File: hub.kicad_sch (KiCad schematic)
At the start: 26 parts, among them J1 USB_C_Receptacle_USB2.0_16P, Q1 2N7002, Q2 2N7002, U1 ADuM4165, U2 USBLC6-2SC6, U3 TLV7042DDFR, Y1 24MHz

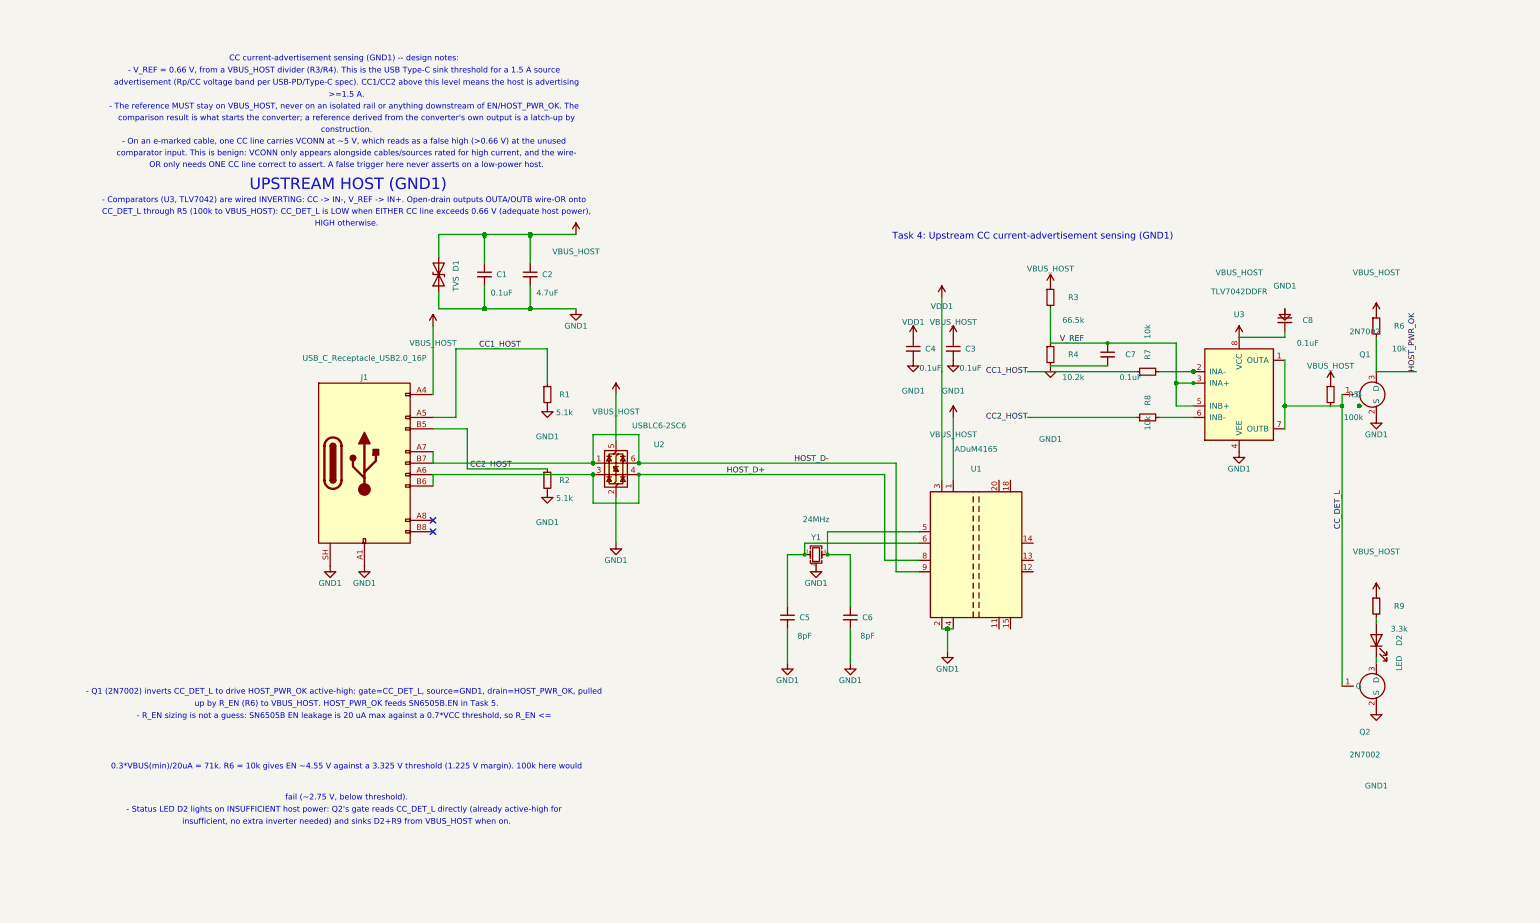
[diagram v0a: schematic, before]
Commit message: feat(revb/sch): SN6505B isolated DC-DC gated by host CC sense
Task 5 of the revb-hub-schematic plan — the isolated power chain and
first GND2-domain circuitry (push-pull converter, rectifier, buck-boost).

- U5 (SN6505BDBV) push-pull driver: VCC/GND on GND1 via C10 (0.1uF bypass)
  + C11 (4.7uF mandatory VCC bulk); EN <- HOST_PWR_OK (the change from both
  predecessor boards, which tied EN to VBUS permanently).
- T1 (750313638) transformer bridges GND1 (primary) to GND2 (secondary,
  CT2 -> GND2). C12 centre-tap bulk trimmed to 0.1uF (see budget below).
- D3/D4 (SS34, Device:D_Schottky) full-wave centre-tap rectifier into
  DCDC_RAW, side by side per the brief.
- U6 (TPS630701RNMR, fixed 5.0V buck-boost) — new custom symbol +
  placeholder footprint in isolator-lib, pin table per the decision
  record's Sec 2.4: FB tied to VOUT via R_FB0=0R (fixed-part requirement,
  not optional); PS/SYNC via R_PSS=100k to ISO_5V_PRE with a DNP 0R pad
  wired to the PS/SYNC node (not to ISO_5V_PRE — rev 2's wording would
  have shorted the rail to GND2 if that pad were ever fitted); EN tied to
  DCDC_RAW, not ISO_5V_PRE; VSEL tied to GND2; PG pulled up 100k; FB2 left
  open. Support caps (C_IN/C_IN-HF/C_OUT/C_OUT-HF/C_VAUX) and inductor L1
  per the decision record's table. R13/R2 (523k/100k) DNP footprints laid
  out for the adjustable-part fallback, tied to the FB node.
- Output net is ISO_5V_PRE (per the decision record's naming, not the
  brief's DCDC_5V — ISO_5V is reserved for the Task 6 TPS2121 output).

Capacitance budget: C1+C2+C3 (4.9uF, Task 3) + C10+C11+C12 (0.1+4.7+0.1)
= 9.8uF on VBUS_HOST, under the 10uF ceiling — C12 was the lever, reduced
from 4.7uF to 0.1uF as the brief anticipated.

Verification: kicad-cli netlist parse gate green after every batch; ERC
79 violations (18 errors), all baseline-consistent (PWR_FLAG-pending on
every new power net plus the pre-existing ones, U1's still-unwired GND2
pins, U6.FB2 correctly left open) — kicad-cli sch erc exits 0. New
to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
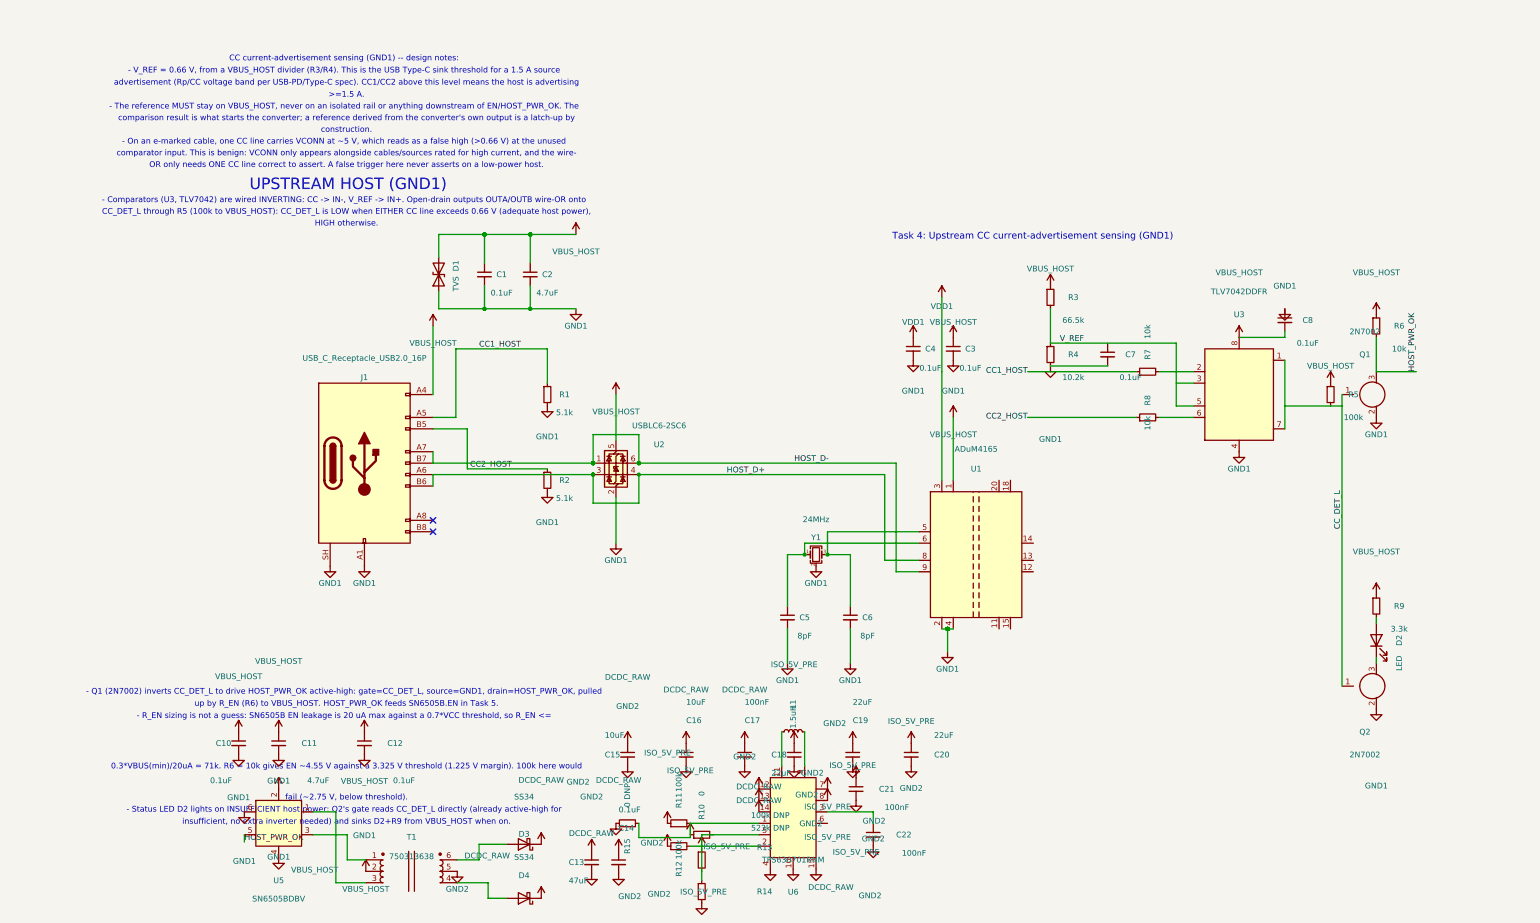
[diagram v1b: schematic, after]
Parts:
- added C10, C12, C14: 0.1uF, symbol Device:C_Small
- added C11: 4.7uF, symbol Device:C_Small
- added C13: 47uF, symbol Device:C_Small
- added C15, C16: 10uF, symbol Device:C_Small
- added C17, C21, C22: 100nF, symbol Device:C_Small
- added C18, C19, C20: 22uF, symbol Device:C_Small
- added D3, D4: SS34, symbol Device:D_Schottky
- added L1: 1.5uH, symbol Device:L_Small
- added R10: 0, symbol Device:R_Small
- added R11, R12: 100k, symbol Device:R_Small
- added R13: 523k DNP, symbol Device:R_Small
- added R14: 100k DNP, symbol Device:R_Small
- added R15: 0 DNP, symbol Device:R_Small
- added T1: 750313638, isolator-lib:WE_750313638, symbol isolator-lib:750313638
- added U5: SN6505BDBV, symbol Power_Management:SN6505BDBV
- added U6: TPS630701RNM, symbol isolator-lib:TPS630701RNM
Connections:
- net CC_DET_L: no longer R5.2, U3.1 (OUTA), U3.7 (OUTB)
- net GND1: now also C10.2, C11.2, C12.2, U5.4 (GND), U5.6 (CLK)
- net GND2: now also C13.2, C14.2, C15.2, C16.2, C17.2, C18.2, C19.2, C20.2, C21.2, C22.2, R14.2, R15.1, T1.5 (CT2), U6.10 (PGND), U6.15 (VSEL), U6.4 (GND)
- net HOST_PWR_OK: now also U5.5 (EN)
- net VBUS_HOST: now also C10.1, C11.1, C12.1, T1.2 (CT1), U5.2 (VCC)
- net V_REF: no longer C7.1, U3.3 (INA+)
- new net: T1.1 (N1), U5.3 (D2)
- new net: T1.3 (N2), U5.1 (D1)
- new net: D4.2 (A), T1.4 (N4)
- new net: D3.2 (A), T1.6 (N3)
- new net: R10.2, R13.2, R14.1, U6.5 (FB)
- new net: R11.2, R15.2, U6.1 (PS/SYNC)
- new net: L1.1, U6.11 (L1)
- new net: R12.2, U6.2 (PG)
- new net: C22.1, U6.3 (VAUX)
- new net: L1.2, U6.9 (L2)
- new net: U3.1 (OUTA), U3.7 (OUTB)
- new net DCDC_RAW: C13.1, C14.1, C15.1, C16.1, C17.1, D3.1 (K), D4.1 (K), U6.12 (VIN), U6.13 (VIN), U6.14 (EN)
- new net ISO_5V_PRE: C18.1, C19.1, C20.1, C21.1, R10.1, R11.1, R12.1, R13.1, U6.7 (VOUT), U6.8 (VOUT)

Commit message: feat(revb/sch): external USB-C input, 3A detect, TPS2121 priority mux
Task 6. Adds J2 (power-only USB-C 6P) with per-CC Rd to GND2, TVS/bulk
caps on EXT_5V, a second TLV7042DDFR 3A-detect instance (1.23V
threshold, GND2 domain) driving the TPS2121 priority mux via a 2N7002
inverter, and the mux itself producing ISO_5V.

Per the corrected decision record (part-selection.md §4.3, overriding
the brief's original Step 3): CP2 is a static bias from IN2
(ISO_5V_PRE) via 23.7k/10.2k -- never driven by the 3A detect, which
was the original error. PR1 is what the 2N7002 inverter drives, via
17.8k/10.0k from EXT_5V. This gives a designed switchback (handback to
the converter) at IN1 ~4.18V nominal, 3.92-4.54V worst-case, recorded
in a schematic text note. Status LED (D6) off the TPS2121 ST pin.

Verification: text-overlap checker 0 overlaps, isolation checker exit
0, ERC shows one new PWR_FLAG-pending error for EXT_5V (same accepted
pattern as every other power net in this file) plus off-grid/lib-
mismatch warnings consistent with existing baseline. ISO_5V_PRE
carries U6's pins/caps, TPS2121 IN2, and the CP2 bias divider (R25) --
the last is an intentional §4.3 requirement, not a mux bypass.

Co-Authored-By: Claude Opus 5 <noreply@anthropic.com>
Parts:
- added C23, C25, C26, C27: 0.1uF, symbol Device:C_Small
- added C24: 4.7uF, symbol Device:C_Small
- added D5: TVS, symbol Device:D_TVS
- added D6: LED, symbol Device:LED
- added J2: USB_C_Receptacle_PowerOnly_6P, symbol Connector:USB_C_Receptacle_PowerOnly_6P
- added Q3: 2N7002, symbol isolator-lib:2N7002
- added R16, R17: 5.1k, symbol Device:R_Small
- added R18: 30.1k, symbol Device:R_Small
- added R19: 9.76k, symbol Device:R_Small
- added R20, R21, R28: 10k, symbol Device:R_Small
- added R22: 100k, symbol Device:R_Small
- added R23: 17.8k, symbol Device:R_Small
- added R24: 10.0k, symbol Device:R_Small
- added R25: 23.7k, symbol Device:R_Small
- added R26: 10.2k, symbol Device:R_Small
- added R27: 35.7k, symbol Device:R_Small
- added R29: 1k, symbol Device:R_Small
- added U7: TLV7042DDFR, symbol isolator-lib:TLV7042DDFR
- added U8: TPS2121, symbol isolator-lib:TPS2121
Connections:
- net GND1: no longer C1.2, C2.2
- net GND2: now also C23.2, C24.2, C25.2, C26.2, C27.2, D5.2 (A2), D6.1 (K), J2.A12 (GND), J2.B12 (GND), J2.SH (SHIELD), Q3.2 (S), R16.2, R17.2, R19.2, R24.2, R26.2, R27.2, U7.4 (VEE), U8.12 (GND), U8.4 (OV2), U8.5 (OV1)
- net ISO_5V_PRE: now also R25.1, U8.2 (IN2)
- net VBUS_HOST: no longer C1.1, C2.1
- new net: R27.1, U8.10 (ILIM)
- new net: C27.1, U8.11 (SS)
- new net: R25.2, R26.1, U8.3 (CP2)
- new net: R28.2, R29.1, U8.9 (ST)
- new net: D6.2 (A), R29.2
- new net: J2.A5 (CC1), R16.1, R20.1
- new net: Q3.1 (G), R22.2, U7.1 (OUTA), U7.7 (OUTB)
- new net: J2.B5 (CC2), R17.1, R21.1
- new net: R21.2, U7.6 (INB-)
- new net: C25.1, R18.2, R19.1, U7.3 (INA+), U7.5 (INB+)
- new net: R20.2, U7.2 (INA-)
- new net EXT_5V: C23.1, C24.1, C26.1, D5.1 (A1), J2.A9 (VBUS), J2.B9 (VBUS), R18.1, R22.1, R23.1, U7.8 (VCC), U8.7 (IN1)
- new net ISO_5V: R28.1, U8.1 (OUT), U8.8 (OUT)
- new net PR1_NODE: Q3.3 (D), R23.2, R24.1, U8.6 (PR1)
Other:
- note added: "CP2 rule (Table 9-3): CP2=hi,PR1=lo selects IN2; CP2=PR1=lo selects VCOMP (higher wins). CP2(pin3)=STATIC bias from ISO_5V_PRE, 23.7k/10.2k to GND2, never the 3A detect."
- note added: "PR1(pin6)=driven by 3A-detect 2N7002 inverter, 17.8k/10.0k EXT_5V to GND2. Switchback: approx 4.18V nominal, worst-case 3.92-4.54V -- measure at bring-up."
- note added: "Task 6: External supply, 3A detect, TPS2121 priority mux (GND2)"
